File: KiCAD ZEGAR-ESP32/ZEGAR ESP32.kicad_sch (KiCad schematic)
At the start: 46 parts, among them Q13 IRLZ44N, Q14 IRLZ44N, Q15 BC547, Q16 BC557, U1 ESP32-WROOM-32D, U12 ESP32-C3-WROOM-02, U13 TC4427xOA, U14 ESP32-C3-WROOM-02, U16 IR2110

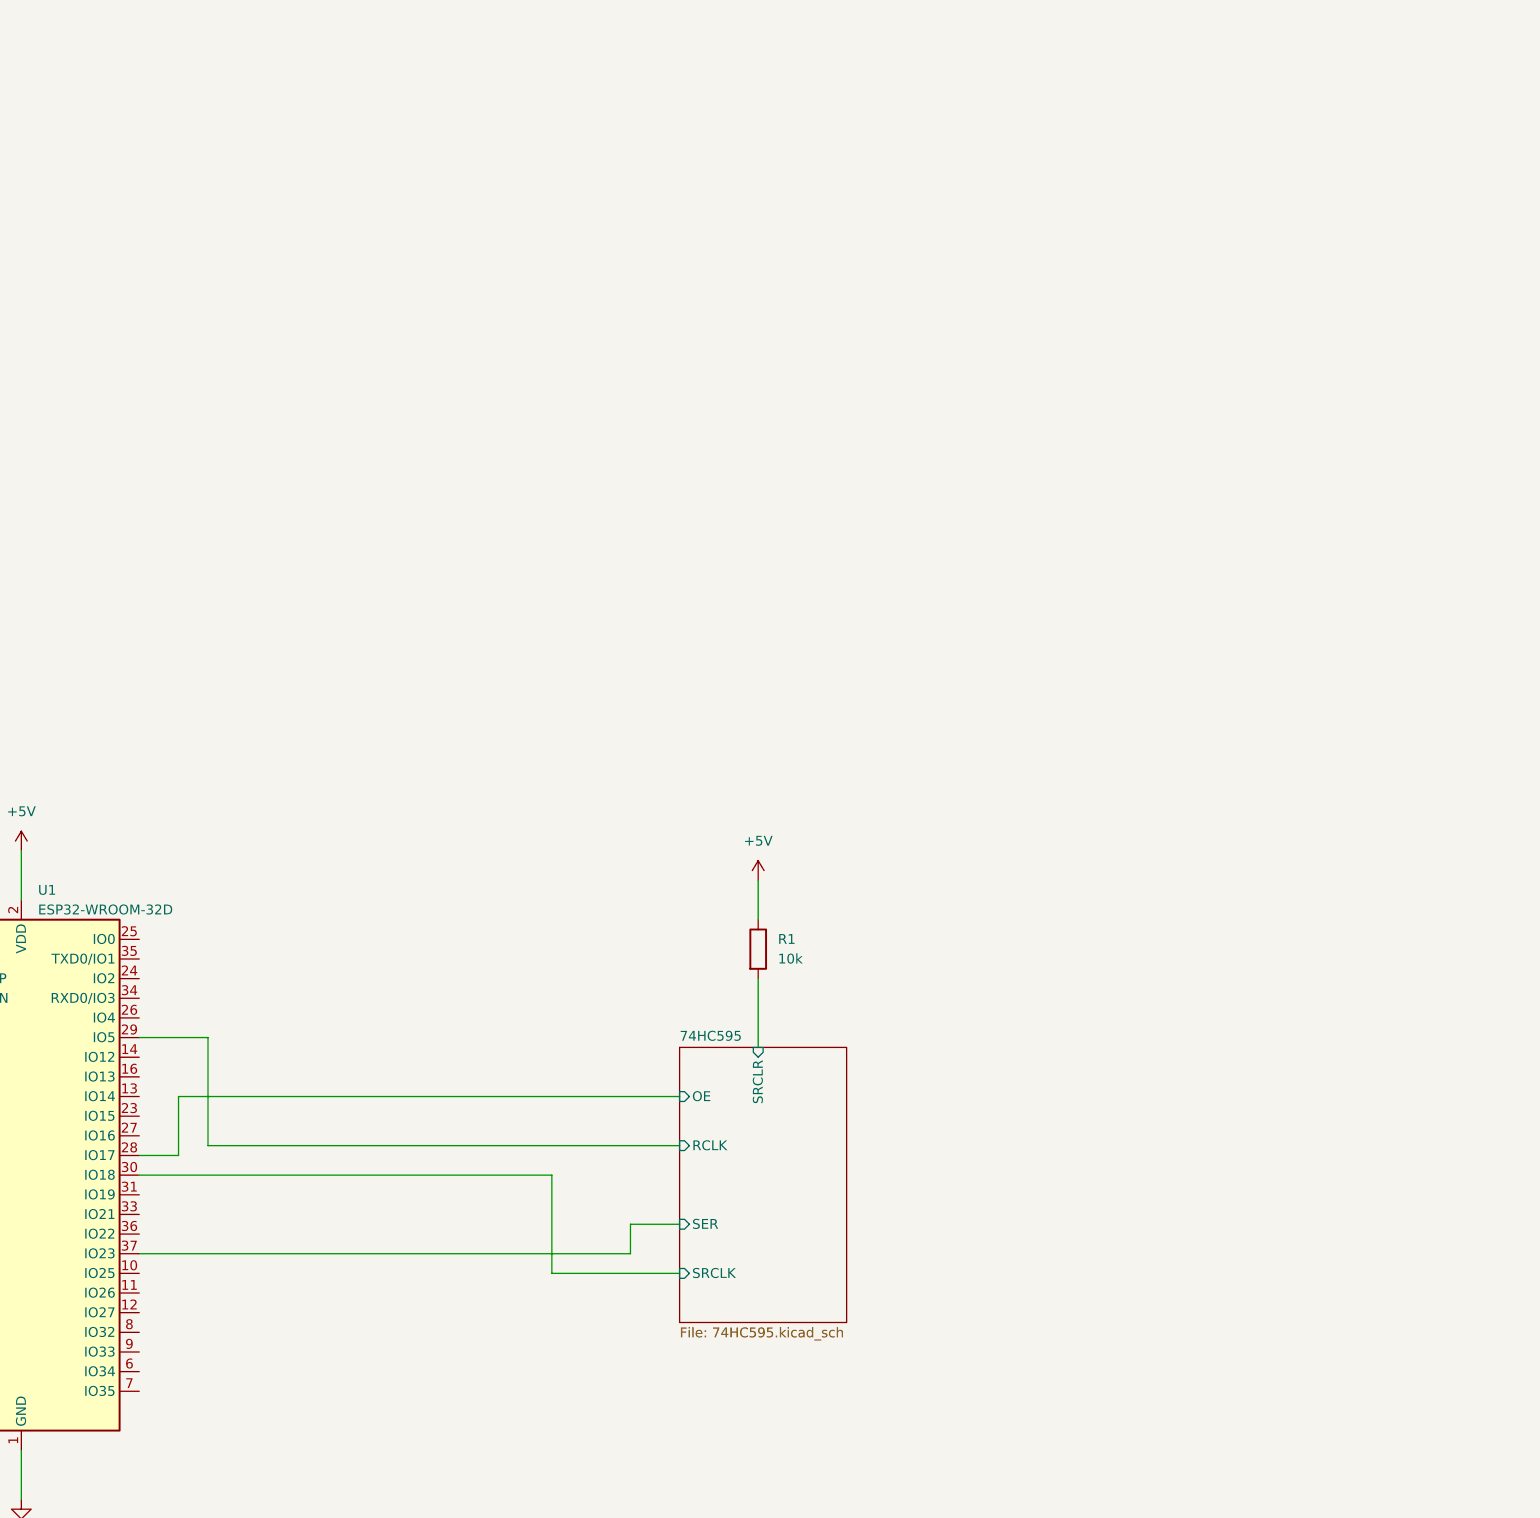
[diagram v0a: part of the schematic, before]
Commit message: V1.12Refactor Bluetooth audio pin configuration and update I2C initialization
- Deleted FirebaseSync.h and FirebaseSync.cpp files as they are no longer needed.
- Updated AudioBT.cpp to change the data output pin for PCM5102 from GPIO22 to GPIO14 for better pin management.
- Modified main.cpp to initialize I2C with explicit SDA and SCL pins (GPIO21 and GPIO22) after ensuring GPIO22 is free from I2S usage.
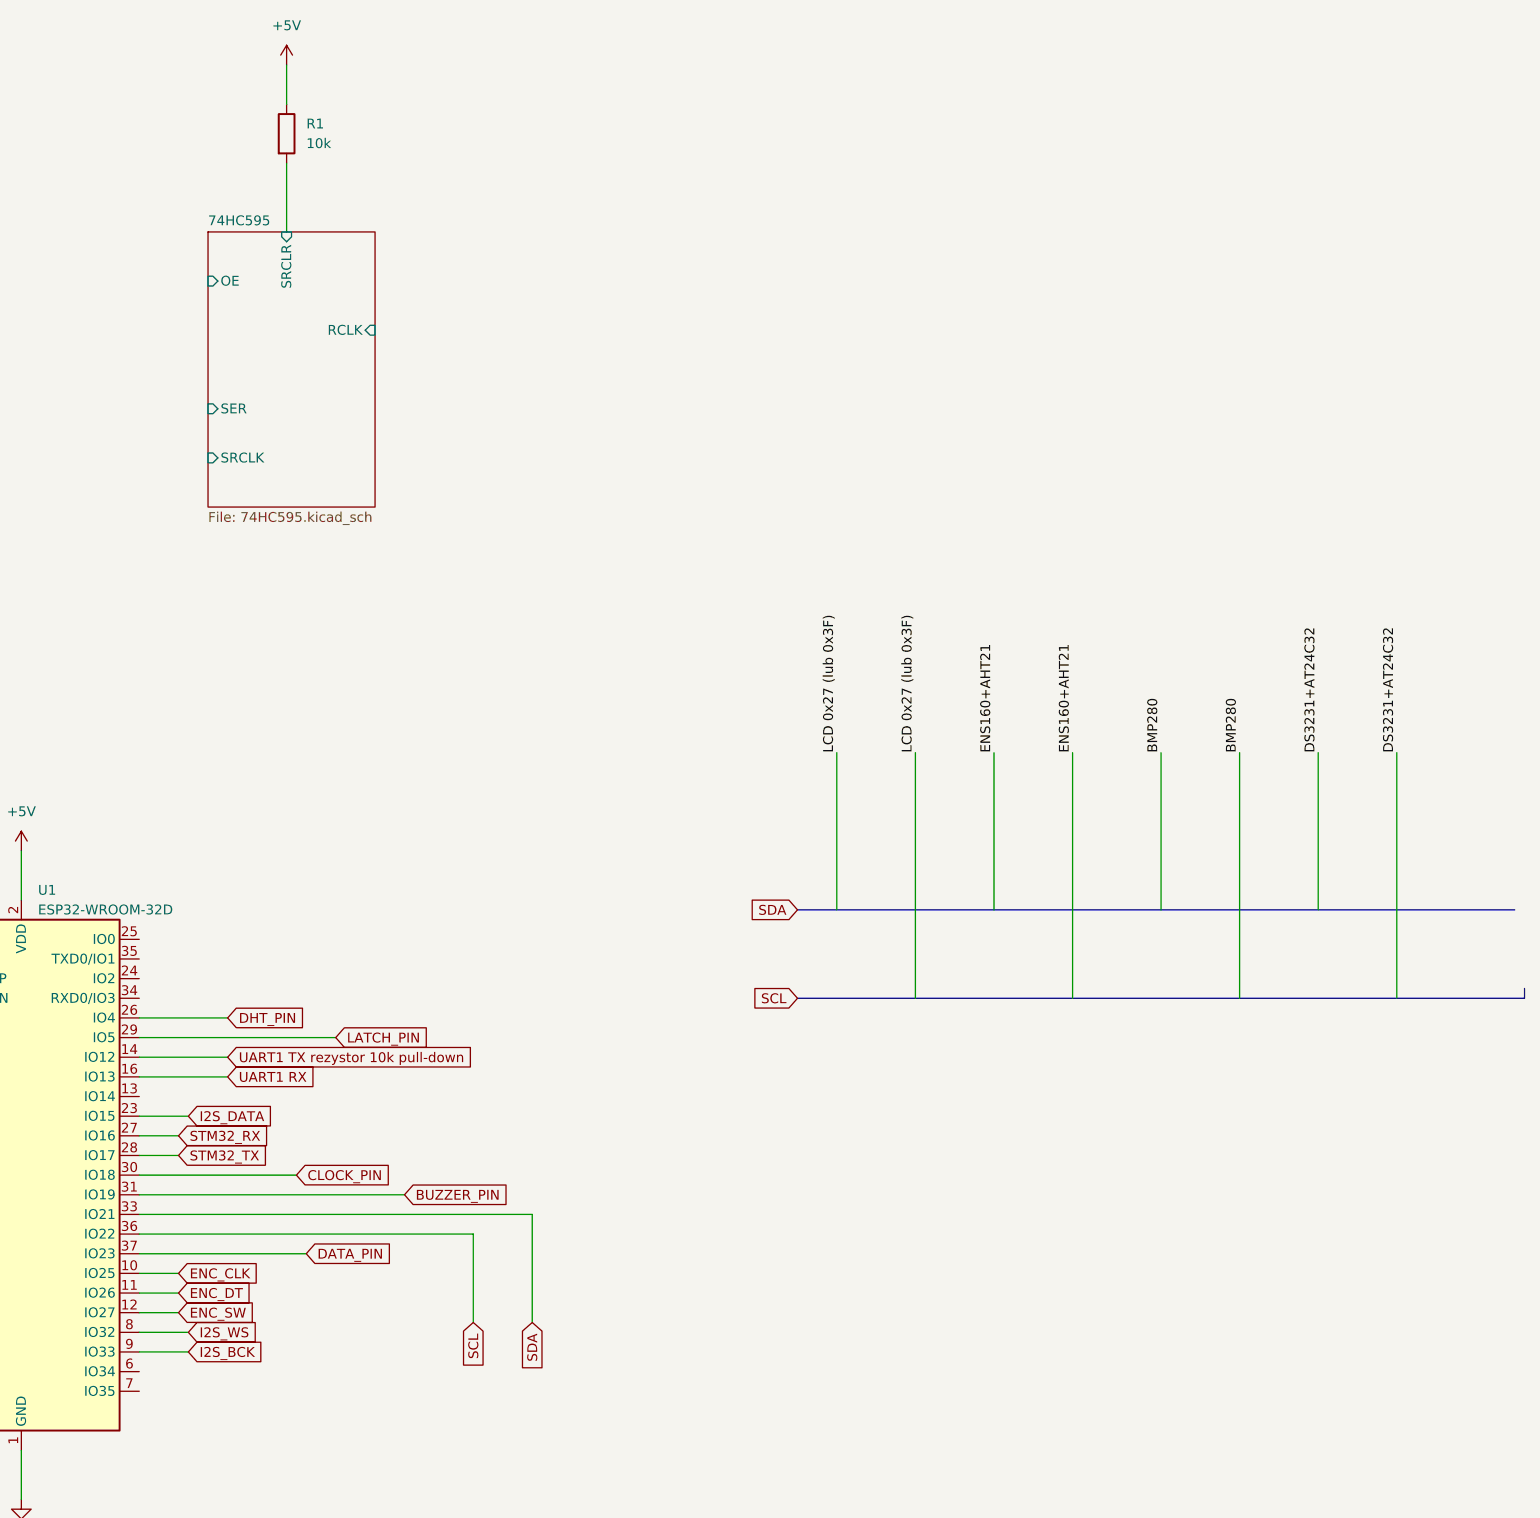
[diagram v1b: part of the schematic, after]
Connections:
- net 74HC595/OE: no longer U1.28 (IO17)
- net 74HC595/RCLK: no longer U1.29 (IO5)
- net 74HC595/SER: no longer U1.37 (IO23)
- net 74HC595/SRCLK: no longer U1.30 (IO18)
- net ENC_CLK: now reaches U1.10 (IO25)
- net ENC_DT: now reaches U1.11 (IO26)
- net ENC_SW: now reaches U1.12 (IO27)
- net UART1 TX rezystor 10k pull-down: now reaches U1.14 (IO12)
- net UART1 RX: now reaches U1.16 (IO13)
- net I2S_DATA: now reaches U1.23 (IO15)
- net DHT_PIN: now reaches U1.26 (IO4)
- net STM32_RX: now reaches U1.27 (IO16)
- net BUZZER_PIN: now reaches U1.31 (IO19)
- net SDA: now reaches U1.33 (IO21)
- net SCL: now reaches U1.36 (IO22)
- net I2S_WS: now reaches U1.8 (IO32)
- net I2S_BCK: now reaches U1.9 (IO33)
- new net CLOCK_PIN: U1.30 (IO18)
- new net DATA_PIN: U1.37 (IO23)
- new net LATCH_PIN: U1.29 (IO5)
- new net STM32_TX: U1.28 (IO17)
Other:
- moved on the sheet: R1

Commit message: V1.22
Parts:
- added U15: ESP32-C3-WROOM-02, RF_Module:ESP32-C3-WROOM-02, symbol RF_Module:ESP32-C3-WROOM-02
- added U17: CC430F5133xRGZ, Package_DFN_QFN:VQFN-48-1EP_7x7mm_P0.5mm_EP4.1x4.1mm_ThermalVias, symbol MCU_Texas_MSP430:CC430F5133xRGZ
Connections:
- new net: U15.19 (GND), U15.9 (GND)
- new net: U17.22 (DVCC), U17.41 (DVCC), U17.8 (DVCC)
- new net: U17.27 (AVCC_RF), U17.28 (AVCC_RF)
- new net: U17.31 (AVCC_RF), U17.32 (AVCC_RF)
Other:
- note added: "CS=3 SCK=6 MOSI=7 MISO=10 GDO0=1 GDO2=0"
